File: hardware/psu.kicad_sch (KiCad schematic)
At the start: 19 parts

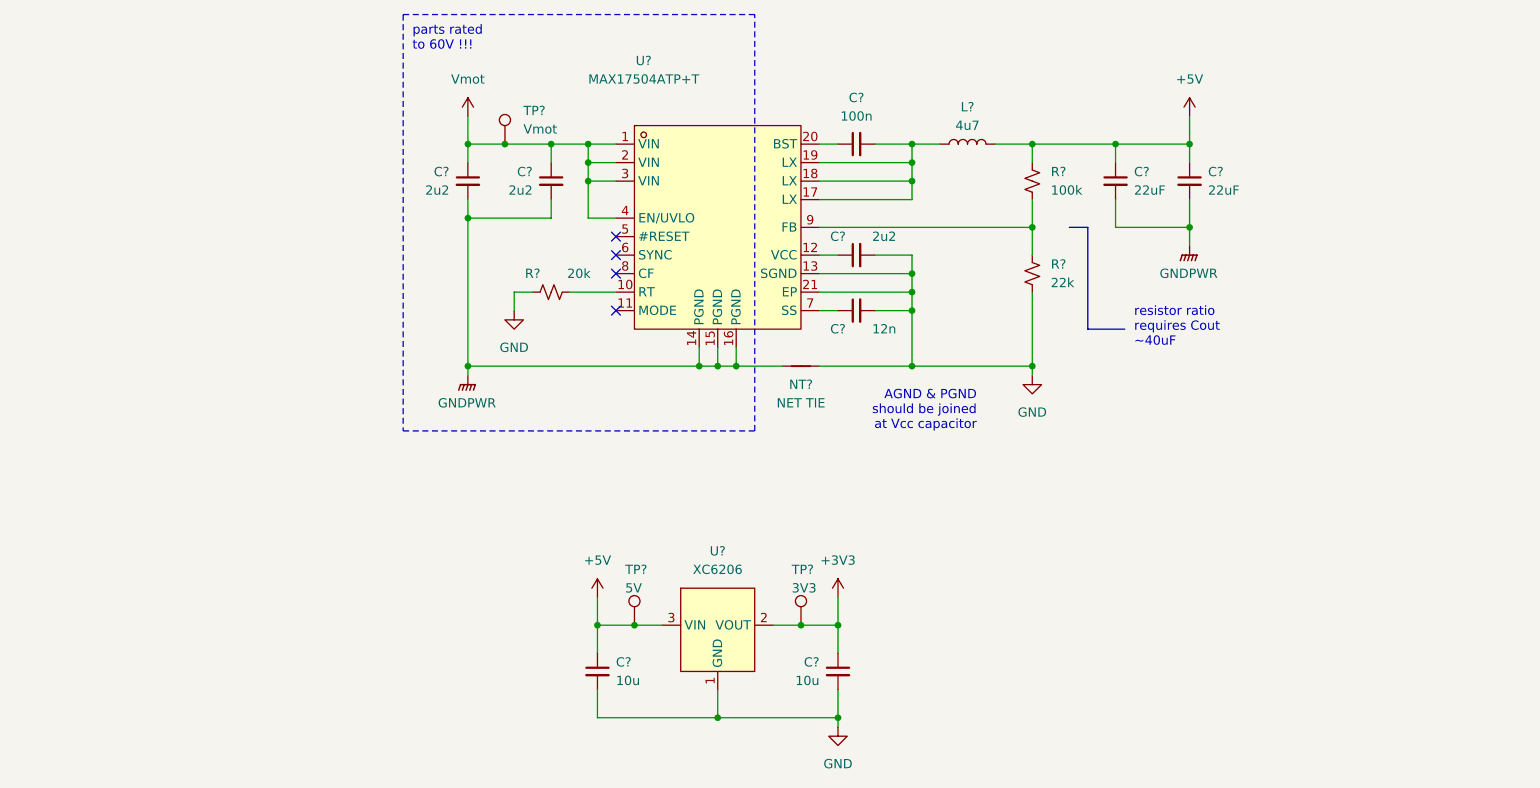
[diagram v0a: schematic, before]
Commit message: finish component selection
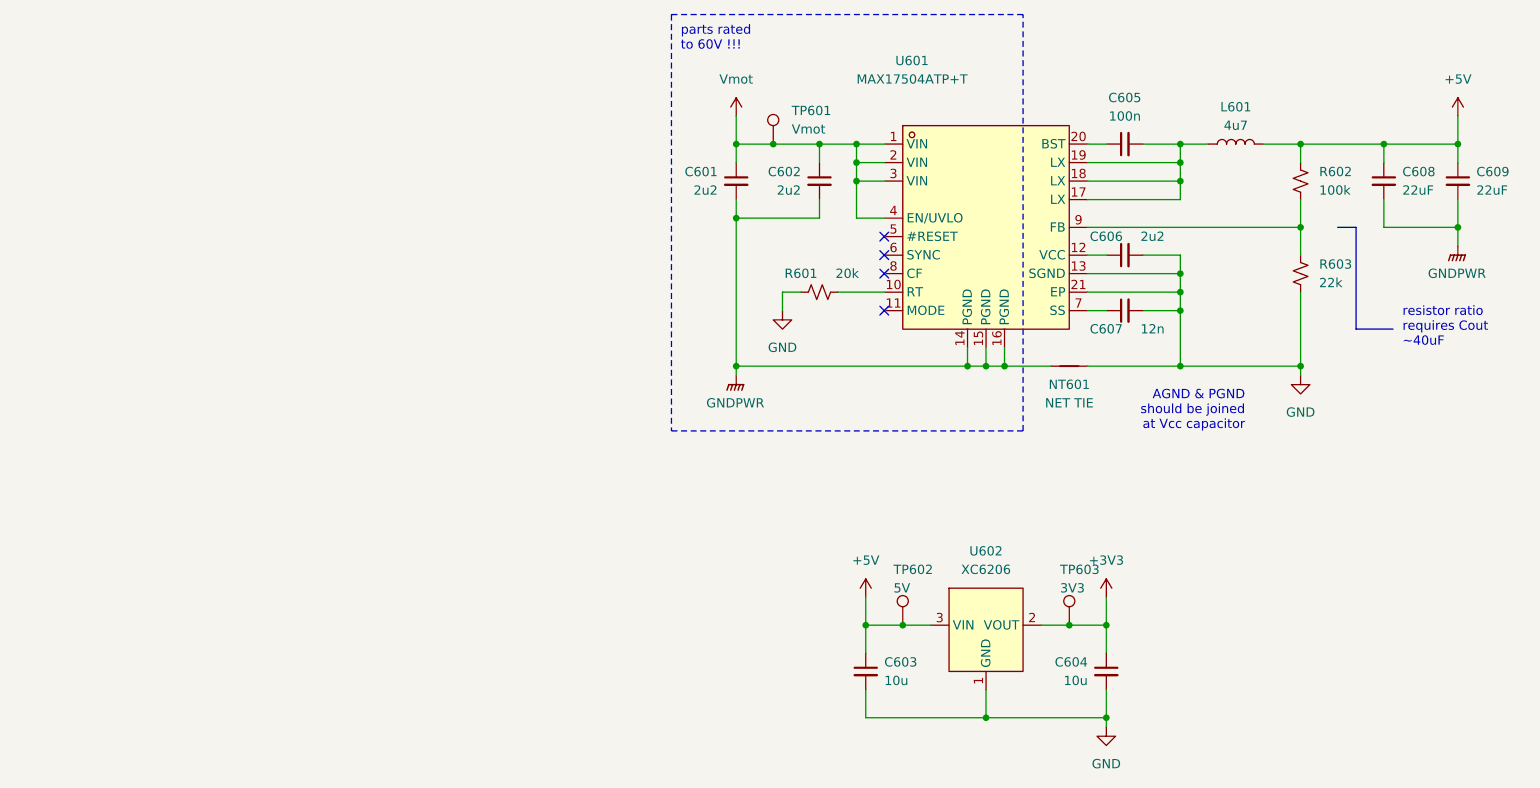
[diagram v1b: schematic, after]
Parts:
- gave numbers to parts that had none: 19
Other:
- moved on the sheet: C601, C602, C603, C604, C605, C606, C607, C608, C609, L601, NT601, R601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

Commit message: try new driver
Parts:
- removed C601, C602, C606: 2u2, Capacitor_SMD:C_0805_2012Metric, symbol Device:C_Small
- removed C603, C604: 10u, Capacitor_SMD:C_0805_2012Metric, symbol Device:C_Small
- removed C605: 100n, Capacitor_SMD:C_0402_1005Metric, symbol Device:C_Small
- removed C607: 12n, Capacitor_SMD:C_0402_1005Metric, symbol Device:C_Small
- removed C608, C609: 22uF, Capacitor_SMD:C_0805_2012Metric, symbol Device:C_Small
- removed L601: 4u7, Inductor_SMD:L_Vishay_IHLP-4040, symbol Device:L
- removed NT601: NET TIE, NetTie:NetTie-2_SMD_Pad2.0mm, symbol Device:NetTie_2
- removed R601: 20k, Resistor_SMD:R_0402_1005Metric, symbol Device:R_Small_US
- removed R602: 100k, Resistor_SMD:R_0402_1005Metric, symbol Device:R_Small_US
- removed R603: 22k, Resistor_SMD:R_0402_1005Metric, symbol Device:R_Small_US
- removed TP601: Vmot, TestPoint:TestPoint_Pad_D1.0mm, symbol Connector:TestPoint
- removed TP602: 5V, TestPoint:TestPoint_Pad_D1.0mm, symbol Connector:TestPoint
- removed TP603: 3V3, TestPoint:TestPoint_Pad_D1.0mm, symbol Connector:TestPoint
- removed U601: MAX17504ATP+T, easyeda2kicad:QFN-20_L5.0-W5.0-P0.65-BL-EP, symbol easyeda2kicad:MAX17504ATP+T
- removed U602: XC6206, Package_TO_SOT_SMD:SOT-23, symbol matei:XC6206
- added C501, C503: 10u, Capacitor_SMD:C_0805_2012Metric, symbol Device:C_Small
- added C502: 1u, Capacitor_SMD:C_0402_1005Metric, symbol Device:C_Small
- added D501, D502: BZT52C30S, Diode_SMD:D_SOD-323, symbol Device:D_Zener
- added L501: 33u, Inductor_SMD:L_1210_3225Metric, symbol Device:L_Small
- added Q501: MMBT5551, Package_TO_SOT_SMD:SOT-23, symbol Transistor_BJT:MMBT5551L
- added R501: 200k, Resistor_SMD:R_0402_1005Metric, symbol Device:R_Small_US
- added R502: 51k, Resistor_SMD:R_0402_1005Metric, symbol Device:R_Small_US
- added R503: 22k, Resistor_SMD:R_0402_1005Metric, symbol Device:R_Small_US
- added R504: 5R, Resistor_SMD:R_0603_1608Metric, symbol Device:R_Small_US
- added R505: 15k, Resistor_SMD:R_0402_1005Metric, symbol Device:R_Small_US
- added U501: MAX15062CATA+T, easyeda2kicad:TDFN-8_L2.0-W2.0-P0.50-BL, symbol easyeda2kicad:MAX15062CATA+T
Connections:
- net +3V3: now also C503.1, L501.2, R501.1
- net GND: now also C501.2, C502.2, C503.2, Q501.2 (E), R503.2, U501.5 (MODE), U501.7 (GND)
- net Vmot: now also C501.1, D501.1 (K), R504.1, U501.1 (VIN), U501.2 (EN/UVLO)
- new net: Q501.1 (B), R505.2
- new net: Q501.3 (C), R504.2
- new net: C502.1, U501.3 (VCC), U501.6 (~{RESET})
- new net: D502.2 (A), R505.1
- new net: R501.2, R502.1, U501.4 (FB/VOUT)
- new net: L501.1, U501.8 (LX)
- new net: D501.2 (A), D502.1 (K)
- new net: R502.2, R503.1
- no-connect marks 4 -> 0
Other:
- note added: "60V breakdown"
- note added: "Ra = Rb(Vout/0.9 - 1) 3.36V (closest to 3v3 with basic parts)"
- note added: "V = IR R = 60V/0.005 = 12K"
- note removed: "AGND & PGND should be joined at Vcc capacitor"
- note removed: "parts rated to 60V !!!"
- note removed: "resistor ratio requires Cout ~40uF"

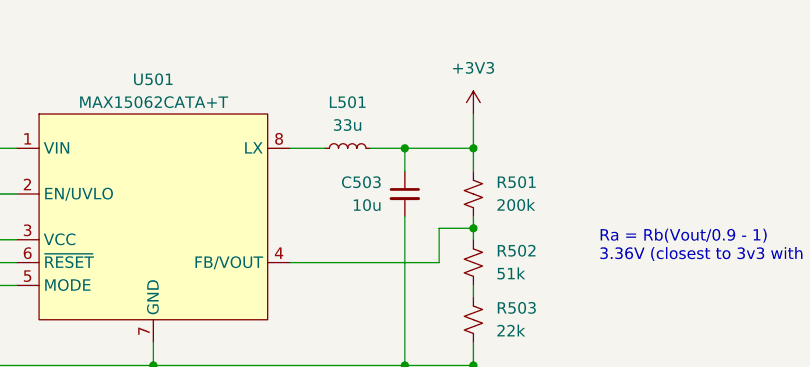
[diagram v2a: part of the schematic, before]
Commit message: clean up ERC in schematic
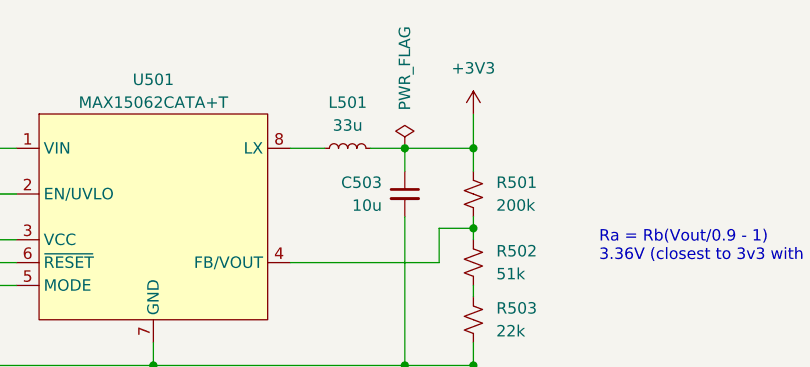
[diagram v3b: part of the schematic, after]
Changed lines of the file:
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@@
+    )
+  )
+  (symbol (lib_id "power:PWR_FLAG") (at 173.99 74.93 0) (unit 1)
+    (in_bom yes) (on_board yes) (dnp no)
+    (property "Reference" "#FLG0501" (at 173.99 73.025 0)
+      (effects (font (size 1.27 1.27)) hide)
+    )
+    (property "Value" "PWR_FLAG" (at 173.99 66.04 90)
+      (effects (font (size 1.27 1.27)))
+    )
+    (property "Footprint" "" (at 173.99 74.93 0)
+      (effects (font (size 1.27 1.27)) hide)
+    )
+    (property "Datasheet" "~" (at 173.99 74.93 0)
+      (effects (font (size 1.27 1.27)) hide)
+    )
+    (pin "1")
+    (instances
+      (project "lemon-pepper"
+        (path "/0306e2fa-4433-4288-91d9-65a3484207ad/1237e3d8-f89f-4b6e-a633-6dbf7c464e03"
+          (reference "#FLG0501") (unit 1)
+        )
+      )
     )
   )

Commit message: fix bringup issues
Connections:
- net at C502.1, U501.3 (VCC): no longer U501.6 (~{RESET})
- no-connect marks 0 -> 1
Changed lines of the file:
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@@
   (junction (at 173.99 74.93) (diameter 0) (color 0 0 0 0)
-  )
-  (junction (at 123.19 87.63) (diameter 0) (color 0 0 0 0)
   )
   (junction (at 173.99 99.06) (diameter 0) (color 0 0 0 0)
@@
   (junction (at 181.61 99.06) (diameter 0) (color 0 0 0 0)
   )
+  (no_connect (at 130.81 87.63))
   (wire (pts (xy 181.61 82.55) (xy 181.61 83.82))
     (stroke (width 0) (type default))
@@
     (stroke (width 0) (type default))
   )
-  (wire (pts (xy 123.19 85.09) (xy 123.19 87.63))
-    (stroke (width 0) (type default))
-  )
   (wire (pts (xy 181.61 83.82) (xy 181.61 85.09))
     (stroke (width 0) (type default))
@@
     (stroke (width 0) (type default))
   )
-  (wire (pts (xy 123.19 87.63) (xy 123.19 91.44))
+  (wire (pts (xy 123.19 85.09) (xy 123.19 91.44))
     (stroke (width 0) (type default))
   )
@@
     (stroke (width 0) (type default))
   )
-  (wire (pts (xy 123.19 87.63) (xy 130.81 87.63))
-    (stroke (width 0) (type default))
-  )

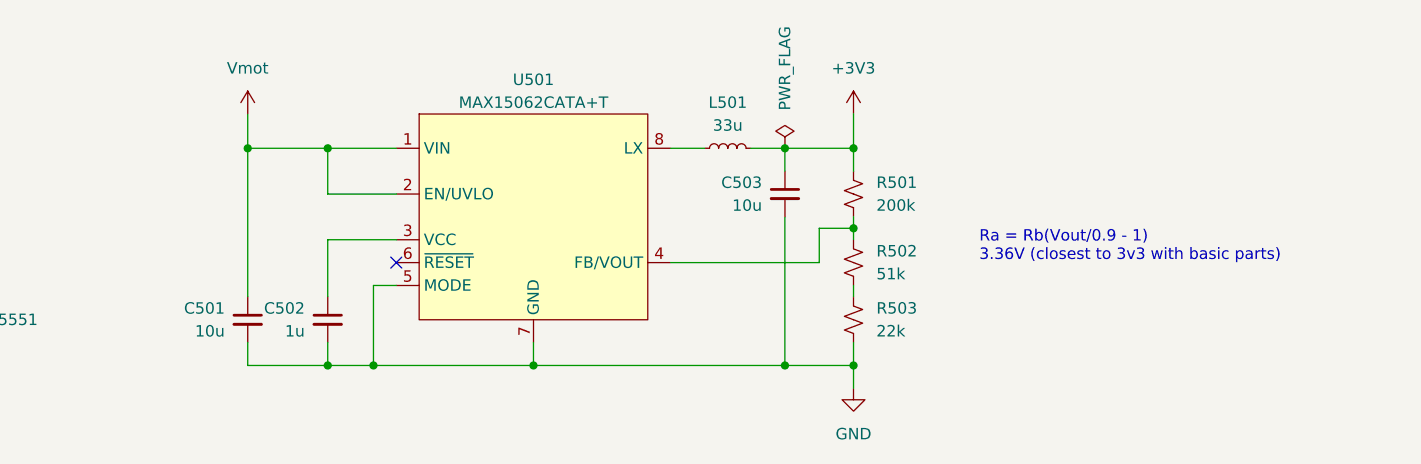
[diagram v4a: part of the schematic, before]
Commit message: start working on current sense
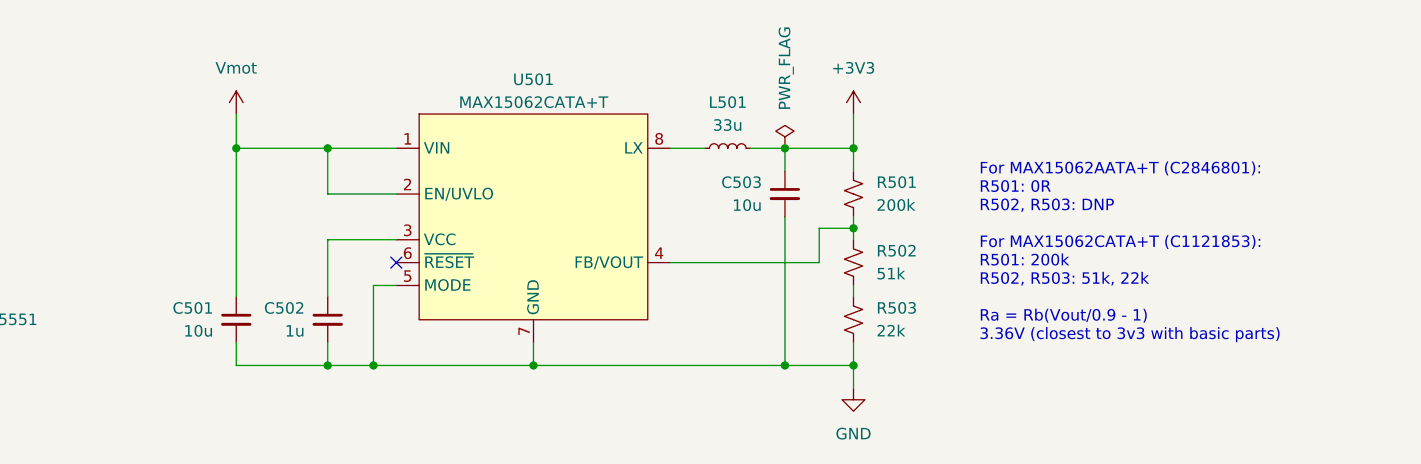
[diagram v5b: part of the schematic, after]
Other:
- note added: "For MAX15062AATA+T (C2846801): R501: 0R R502, R503: DNP For MAX15062CATA+T (C1121853): R501: 200k R502, R503: 51k, 22k Ra = Rb(Vout/0.9 - 1) 3.36V (closest to 3v3 with basic parts)"
- note removed: "Ra = Rb(Vout/0.9 - 1) 3.36V (closest to 3v3 with basic parts)"
- moved on the sheet: C501
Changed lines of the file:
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@@
   (junction (at 146.05 99.06) (diameter 0) (color 0 0 0 0)
   )
-  (junction (at 114.3 74.93) (diameter 0) (color 0 0 0 0)
+  (junction (at 113.03 74.93) (diameter 0) (color 0 0 0 0)
   )
   (junction (at 173.99 74.93) (diameter 0) (color 0 0 0 0)
@@
     (stroke (width 0) (type default))
   )
-  (wire (pts (xy 114.3 74.93) (xy 114.3 91.44))
+  (wire (pts (xy 113.03 74.93) (xy 113.03 91.44))
     (stroke (width 0) (type default))
   )
@@
     (stroke (width 0) (type default))
   )
-  (wire (pts (xy 114.3 96.52) (xy 114.3 99.06))
-    (stroke (width 0) (type default))
-  )
-  (wire (pts (xy 114.3 74.93) (xy 123.19 74.93))
+  (wire (pts (xy 113.03 96.52) (xy 113.03 99.06))
+    (stroke (width 0) (type default))
+  )
+  (wire (pts (xy 113.03 74.93) (xy 123.19 74.93))
     (stroke (width 0) (type default))
   )
@@
     (stroke (width 0) (type default))
   )
-  (wire (pts (xy 114.3 99.06) (xy 123.19 99.06))
+  (wire (pts (xy 113.03 99.06) (xy 123.19 99.06))
     (stroke (width 0) (type default))
   )
@@
     (stroke (width 0) (type default))
   )
-  (wire (pts (xy 114.3 71.12) (xy 114.3 74.93))
+  (wire (pts (xy 113.03 71.12) (xy 113.03 74.93))
     (stroke (width 0) (type default))
   )
@@
     (effects (font (size 1.27 1.27)) (justify left bottom))
   )
-  (text "Ra = Rb(Vout/0.9 - 1)\n3.36V (closest to 3v3 with basic parts)"
-    (at 195.58 87.63 0)
+  (text "For MAX15062AATA+T (C2846801): \nR501: 0R\nR502, R503: DNP\n\nFor MAX15062CATA+T (C1121853):\nR501: 200k\nR502, R503: 51k, 22k\n\nRa = Rb(Vout/0.9 - 1)\n3.36V (closest to 3v3 with basic parts)"
+    (at 195.58 96.52 0)
     (effects (font (size 1.27 1.27)) (justify left bottom))
   )
@@
     (effects (font (size 1.27 1.27)) (justify left bottom))
   )
-  (symbol (lib_id "matei:Vmot") (at 114.3 71.12 0) (unit 1)
-    (in_bom yes) (on_board yes) (dnp no) (fields_autoplaced)
-    (property "Reference" "#PWR0501" (at 109.22 74.93 0)
-      (effects (font (size 1.27 1.27)) hide)
-    )
-    (property "Value" "Vmot" (at 114.3 66.04 0)
-      (effects (font (size 1.27 1.27)))
-    )
-    (property "Footprint" "" (at 114.3 71.12 0)
-      (effects (font (size 1.27 1.27)) hide)
-    )
-    (property "Datasheet" "" (at 114.3 71.12 0)
+  (symbol (lib_id "matei:Vmot") (at 113.03 71.12 0) (unit 1)
+    (in_bom yes) (on_board yes) (dnp no) (fields_autoplaced)
+    (property "Reference" "#PWR0501" (at 107.95 74.93 0)
+      (effects (font (size 1.27 1.27)) hide)
+    )
+    (property "Value" "Vmot" (at 113.03 66.04 0)
+      (effects (font (size 1.27 1.27)))
+    )
+    (property "Footprint" "" (at 113.03 71.12 0)
+      (effects (font (size 1.27 1.27)) hide)
+    )
+    (property "Datasheet" "" (at 113.03 71.12 0)
       (effects (font (size 1.27 1.27)) hide)
     )
@@
     )
   )
-  (symbol (lib_id "Device:C_Small") (at 114.3 93.98 0) (unit 1)
+  (symbol (lib_id "Device:C_Small") (at 113.03 93.98 0) (unit 1)
     (in_bom yes) (on_board yes) (dnp no)
-    (property "Reference" "C501" (at 111.76 92.7163 0)
+    (property "Reference" "C501" (at 110.49 92.7163 0)
       (effects (font (size 1.27 1.27)) (justify right))
     )
-    (property "Value" "10u" (at 111.76 95.2563 0)
+    (property "Value" "10u" (at 110.49 95.2563 0)
       (effects (font (size 1.27 1.27)) (justify right))
     )
-    (property "Footprint" "Capacitor_SMD:C_0805_2012Metric" (at 114.3 93.98 0)
-      (effects (font (size 1.27 1.27)) hide)
-    )
-    (property "Datasheet" "~" (at 114.3 93.98 0)
-      (effects (font (size 1.27 1.27)) hide)
-    )
-    (property "LCSC Part" "C440198" (at 114.3 93.98 0)
-      (effects (font (size 1.27 1.27)) hide)
-    )
+    (property "Footprint" "Capacitor_SMD:C_0805_2012Metric" (at 113.03 93.98 0)
+      (effects (font (size 1.27 1.27)) hide)
+    )
+    (property "Datasheet" "~" (at 113.03 93.98 0)
+      (effects (font (size 1.27 1.27)) hide)
+    )
+    (property "LCSC Part" "C440198" (at 113.03 93.98 0)
+      (effects (font (size 1.27 1.27)) hide)
+    )

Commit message: finalize v3 files
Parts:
- R501: value 200k -> 0R; LCSC Part C25764 -> C17168
- R502, R503: now not fitted; now left out of the parts list
- U501: value MAX15062CATA+T -> MAX15062AATA+T; LCSC Part C1121853 -> C2846801
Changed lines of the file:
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@@
       (effects (font (size 1.27 1.27)))
     )
-    (property "Value" "MAX15062CATA+T" (at 146.05 69.85 0)
+    (property "Value" "MAX15062AATA+T" (at 146.05 69.85 0)
       (effects (font (size 1.27 1.27)))
     )
@@
       (effects (font (size 1.27 1.27)) hide)
     )
-    (property "LCSC Part" "C1121853" (at 146.05 101.6 0)
+    (property "LCSC Part" "C2846801" (at 146.05 101.6 0)
       (effects (font (size 1.27 1.27)) hide)
     )
@@
   )
   (symbol (lib_id "Device:R_Small_US") (at 181.61 93.98 0) (unit 1)
-    (in_bom yes) (on_board yes) (dnp no) (fields_autoplaced)
+    (in_bom no) (on_board yes) (dnp yes) (fields_autoplaced)
     (property "Reference" "R503" (at 184.15 92.71 0)
       (effects (font (size 1.27 1.27)) (justify left))
@@
   )
   (symbol (lib_id "Device:R_Small_US") (at 181.61 87.63 0) (unit 1)
-    (in_bom yes) (on_board yes) (dnp no) (fields_autoplaced)
+    (in_bom no) (on_board yes) (dnp yes) (fields_autoplaced)
     (property "Reference" "R502" (at 184.15 86.36 0)
       (effects (font (size 1.27 1.27)) (justify left))
@@
       (effects (font (size 1.27 1.27)) (justify left))
     )
-    (property "Value" "200k" (at 184.15 81.28 0)
+    (property "Value" "0R" (at 184.15 81.28 0)
       (effects (font (size 1.27 1.27)) (justify left))
     )
@@
       (effects (font (size 1.27 1.27)) hide)
     )
-    (property "LCSC Part" "C25764" (at 181.61 80.01 0)
-      (effects (font (size 1.27 1.27)) hide)
-    )
+    (property "LCSC Part" "C17168" (at 181.61 80.01 0)
+      (effects (font (size 1.27 1.27)) hide)
+    )
